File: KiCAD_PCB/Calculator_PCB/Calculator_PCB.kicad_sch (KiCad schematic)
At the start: 105 parts

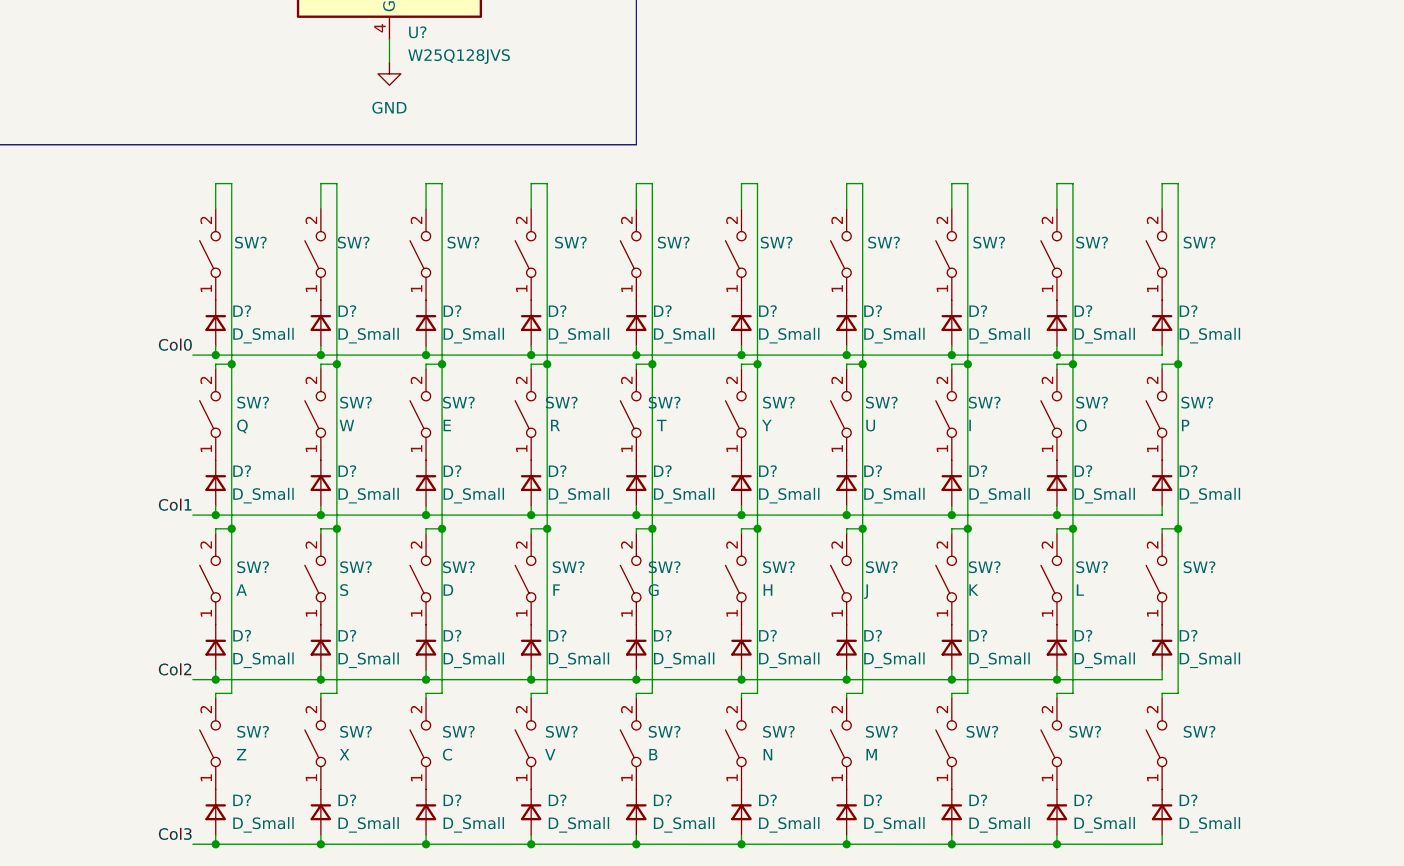
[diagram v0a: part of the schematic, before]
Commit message: PCB Updates
Defining Matrix
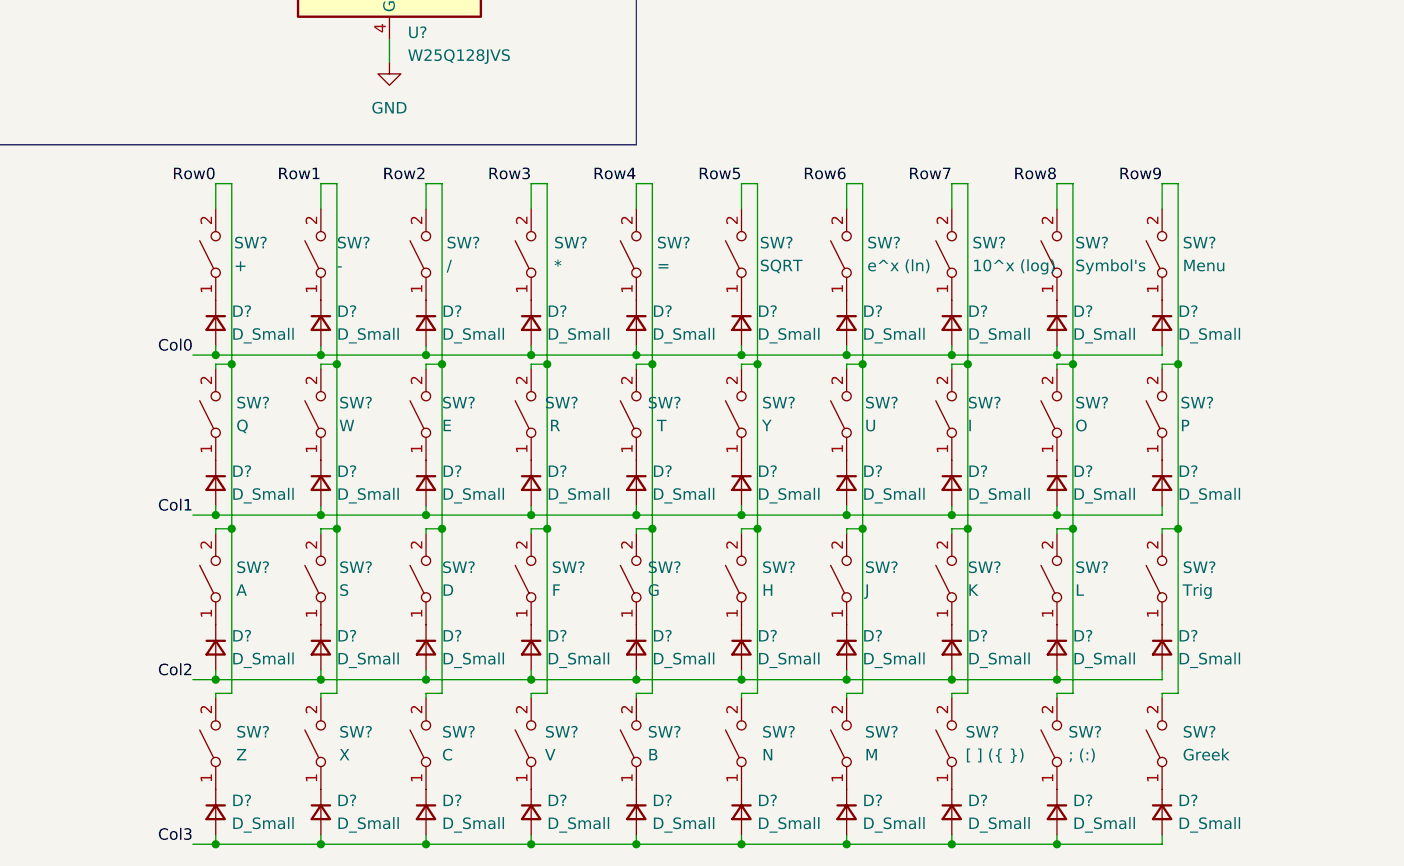
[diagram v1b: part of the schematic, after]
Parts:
- SW?: value (none) -> *
- SW?: value (none) -> ; (:)
- SW?: value (none) -> -
- SW?: value (none) -> Menu
- SW?: value (none) -> SQRT
- SW?: value (none) -> Trig
- SW?: value (none) -> Greek
- SW?: value (none) -> Symbol's
- SW?: value (none) -> e^x (ln)
- SW?: value (none) -> =
- SW?: value (none) -> /
- SW?: value (none) -> [ ] ({ })
- SW?: value (none) -> 10^x (log)
- SW?: value (none) -> +
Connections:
- net Row6: now reaches SW?.2 (B), SW?.2 (B), SW?.2 (B), SW?.2 (B)
- net Row0: now reaches SW?.2 (B), SW?.2 (B), SW?.2 (B), SW?.2 (B)
- net Row3: now reaches SW?.2 (B), SW?.2 (B), SW?.2 (B), SW?.2 (B)
- net Row8: now reaches SW?.2 (B), SW?.2 (B), SW?.2 (B), SW?.2 (B)
- net Row4: now reaches SW?.2 (B), SW?.2 (B), SW?.2 (B), SW?.2 (B)
- net Row1: now reaches SW?.2 (B), SW?.2 (B), SW?.2 (B), SW?.2 (B)
- net Row5: now reaches SW?.2 (B), SW?.2 (B), SW?.2 (B), SW?.2 (B)
- net Row9: now reaches SW?.2 (B), SW?.2 (B), SW?.2 (B), SW?.2 (B)
- net Row2: now reaches SW?.2 (B), SW?.2 (B), SW?.2 (B), SW?.2 (B)
- net Row7: now reaches SW?.2 (B), SW?.2 (B), SW?.2 (B), SW?.2 (B)
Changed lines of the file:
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@@
+    (effects (font (size 1.27 1.27)) (justify right bottom))
+  )
+  (label "Row6" (at 107.442 120.142 180)
+    (effects (font (size 1.27 1.27)) (justify right bottom))
+  )
+  (label "Row2" (at 60.706 120.142 180)
     (effects (font (size 1.27 1.27)) (justify right bottom))
   )
@@
     (effects (font (size 1.27 1.27)) (justify left bottom))
   )
+  (label "Row0" (at 37.338 120.142 180)
+    (effects (font (size 1.27 1.27)) (justify right bottom))
+  )
   (label "Col1" (at 34.798 156.972 180)
     (effects (font (size 1.27 1.27)) (justify right bottom))
@@
     (effects (font (size 1.27 1.27)) (justify left bottom))
   )
+  (label "Row5" (at 95.758 120.142 180)
+    (effects (font (size 1.27 1.27)) (justify right bottom))
+  )
   (label "XIN" (at 272.542 29.972 0)
     (effects (font (size 1.27 1.27)) (justify left bottom))
   )
+  (label "Row1" (at 49.022 120.142 180)
+    (effects (font (size 1.27 1.27)) (justify right bottom))
+  )
+  (label "Row8" (at 130.81 120.142 180)
+    (effects (font (size 1.27 1.27)) (justify right bottom))
+  )
   (label "QSPI_SCLK" (at 33.782 96.52 0)
     (effects (font (size 1.27 1.27)) (justify left bottom))
@@
     (effects (font (size 1.27 1.27)) (justify left bottom))
   )
+  (label "Row3" (at 72.39 120.142 180)
+    (effects (font (size 1.27 1.27)) (justify right bottom))
+  )
   (label "Col2" (at 34.798 175.26 180)
     (effects (font (size 1.27 1.27)) (justify right bottom))
   )
+  (label "Row9" (at 142.494 120.142 180)
+    (effects (font (size 1.27 1.27)) (justify right bottom))
+  )
+  (label "Row7" (at 119.126 120.142 180)
+    (effects (font (size 1.27 1.27)) (justify right bottom))
+  )
   (label "XOUT" (at 272.542 37.084 0)
     (effects (font (size 1.27 1.27)) (justify left bottom))
@@
   (label "USB_D-" (at 276.86 108.458 0)
     (effects (font (size 1.27 1.27)) (justify left bottom))
+  )
+  (label "Row4" (at 84.074 120.142 180)
+    (effects (font (size 1.27 1.27)) (justify right bottom))
   )
   (global_label "IOVDD_49" (shape input) (at 250.698 100.838 0) (fields_autoplaced)
@@
       (effects (font (size 1.27 1.27)) (justify right))
     )
-    (property "Value" "" (id 1) (at 74.93 129.286 90)
+    (property "Value" "*" (id 1) (at 74.93 129.286 90)
       (effects (font (size 1.27 1.27)) (justify right))
     )
@@
       (effects (font (size 1.27 1.27)) (justify right))
     )
-    (property "Value" "" (id 1) (at 132.08 183.6419 90)
+    (property "Value" "; (:)" (id 1) (at 132.08 183.6419 90)
       (effects (font (size 1.27 1.27)) (justify right))
     )
@@
       (effects (font (size 1.27 1.27)) (justify right))
     )
-    (property "Value" "" (id 1) (at 50.8 129.2859 90)
+    (property "Value" "-" (id 1) (at 50.8 129.2859 90)
       (effects (font (size 1.27 1.27)) (justify right))
     )
@@
       (effects (font (size 1.27 1.27)) (justify right))
     )
-    (property "Value" "" (id 1) (at 144.78 129.2859 90)
+    (property "Value" "Menu" (id 1) (at 144.78 129.2859 90)
       (effects (font (size 1.27 1.27)) (justify right))
     )
@@
       (effects (font (size 1.27 1.27)) (justify right))
     )
-    (property "Value" "" (id 1) (at 97.79 129.2859 90)
+    (property "Value" "SQRT" (id 1) (at 97.79 129.2859 90)
       (effects (font (size 1.27 1.27)) (justify right))
     )
@@
       (effects (font (size 1.27 1.27)) (justify right))
     )
-    (property "Value" "" (id 1) (at 144.78 165.3539 90)
+    (property "Value" "Trig" (id 1) (at 144.78 165.3539 90)
       (effects (font (size 1.27 1.27)) (justify right))
     )
@@
       (effects (font (size 1.27 1.27)) (justify right))
     )
-    (property "Value" "" (id 1) (at 144.78 183.6419 90)
+    (property "Value" "Greek" (id 1) (at 144.78 183.6419 90)
       (effects (font (size 1.27 1.27)) (justify right))
     )
@@
       (effects (font (size 1.27 1.27)) (justify right))
     )
-    (property "Value" "" (id 1) (at 132.842 129.286 90)
+    (property "Value" "Symbol's" (id 1) (at 132.842 129.286 90)
       (effects (font (size 1.27 1.27)) (justify right))
     )
@@
       (effects (font (size 1.27 1.27)) (justify right))
     )
-    (property "Value" "" (id 1) (at 109.728 129.286 90)
+    (property "Value" "e^x (ln)" (id 1) (at 109.728 129.286 90)
       (effects (font (size 1.27 1.27)) (justify right))
     )
@@
       (effects (font (size 1.27 1.27)) (justify right))
     )
-    (property "Value" "" (id 1) (at 86.36 129.2859 90)
+    (property "Value" "=" (id 1) (at 86.36 129.2859 90)
       (effects (font (size 1.27 1.27)) (justify right))
     )
@@
       (effects (font (size 1.27 1.27)) (justify right))
     )
-    (property "Value" "" (id 1) (at 62.992 129.286 90)
+    (property "Value" "/" (id 1) (at 62.992 129.286 90)
       (effects (font (size 1.27 1.27)) (justify right))
     )
@@
       (effects (font (size 1.27 1.27)) (justify right))
     )
-    (property "Value" "" (id 1) (at 120.65 183.6419 90)
+    (property "Value" "[ ] ({ })" (id 1) (at 120.65 183.6419 90)
       (effects (font (size 1.27 1.27)) (justify right))
     )
@@
       (effects (font (size 1.27 1.27)) (justify right))
     )
-    (property "Value" "" (id 1) (at 121.412 129.286 90)
+    (property "Value" "10^x (log)" (id 1) (at 121.412 129.286 90)
       (effects (font (size 1.27 1.27)) (justify right))
     )
@@
       (effects (font (size 1.27 1.27)) (justify right))
     )
-    (property "Value" "" (id 1) (at 39.37 129.2859 90)
-      (effects (font (size 1.27 1.27)) (justify right))
-    )
+    (property "Value" "+" (id 1) (at 39.37 129.2859 90)
+      (effects (font (size 1.27 1.27)) (justify right))
+    )

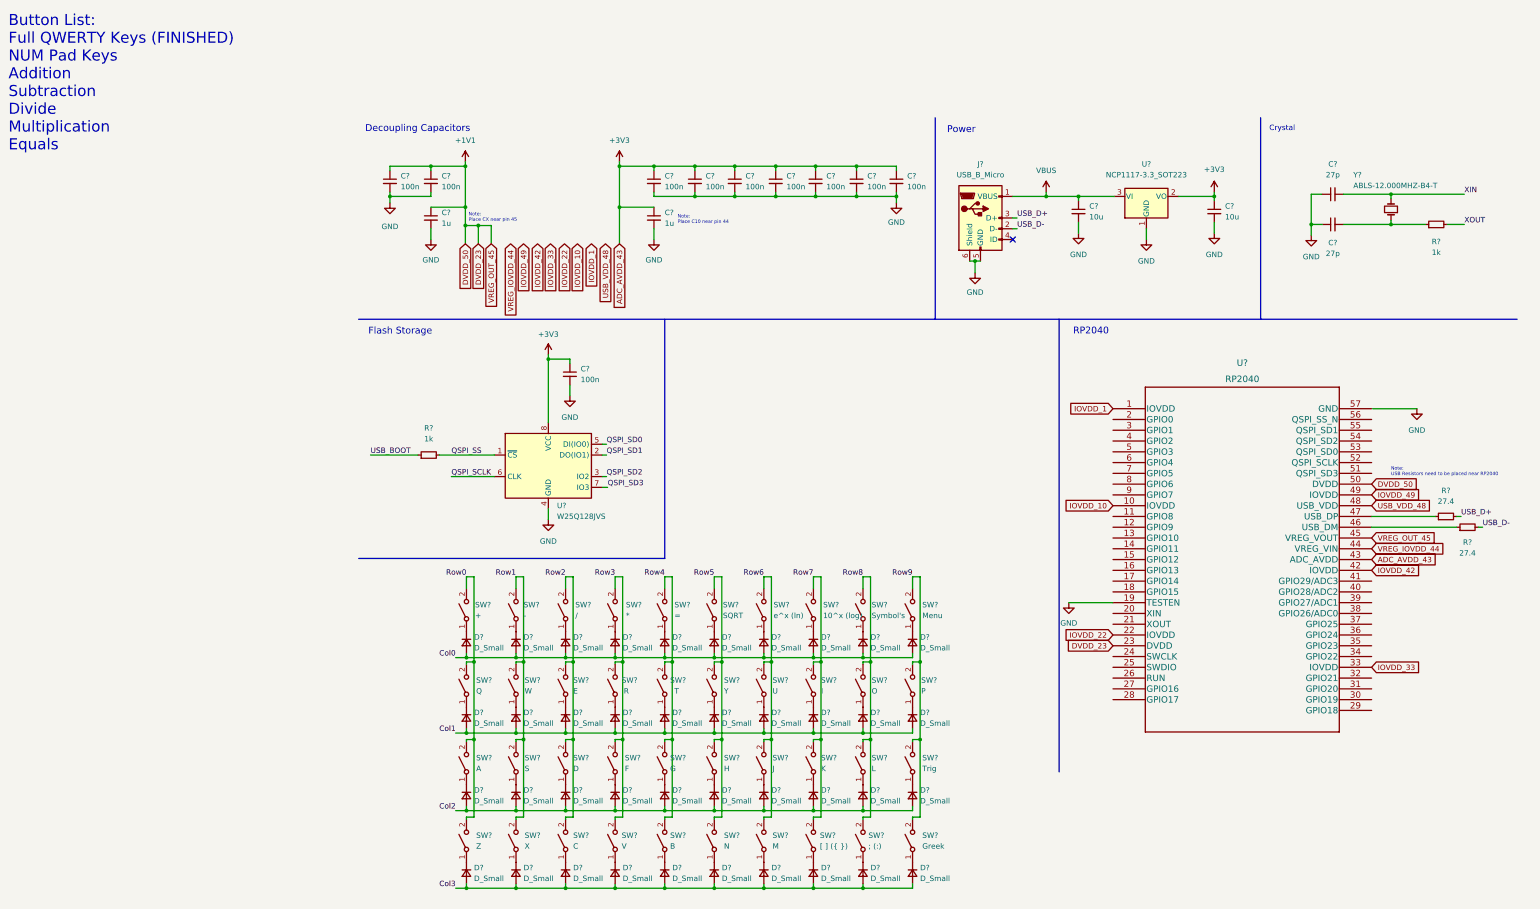
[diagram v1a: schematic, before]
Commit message: PCB Updates
Annotations added
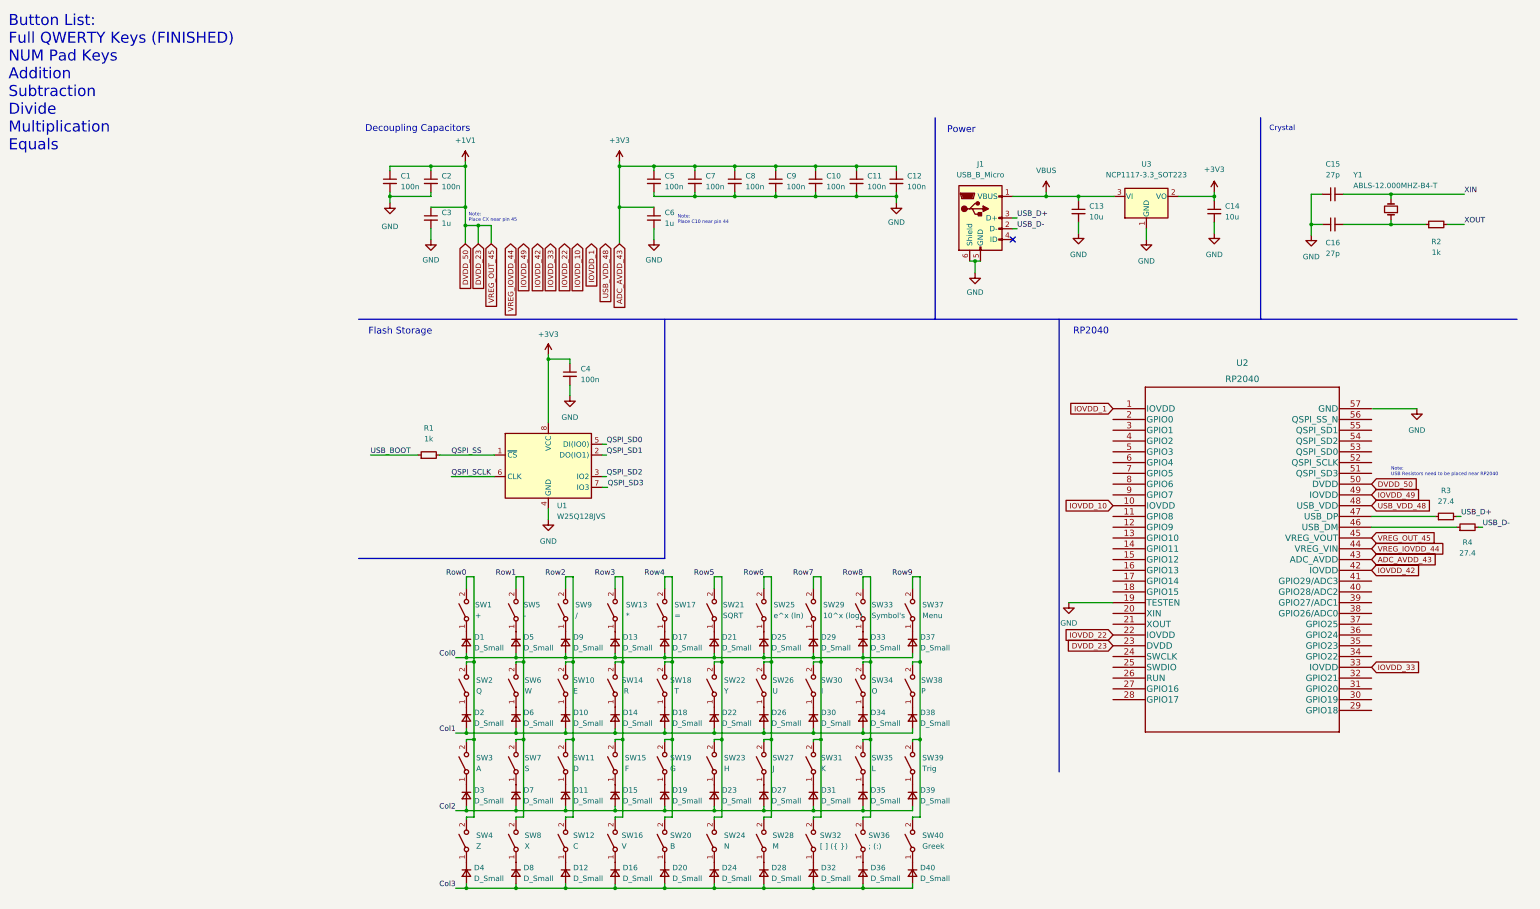
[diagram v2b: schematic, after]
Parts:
- gave numbers to parts that had none: 105

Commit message: PCB Updates
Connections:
- net IOVDD_1 is gone; now on net +3V3: U2.1 (IOVDD)
- net IOVDD_10 is gone; now on net +3V3: U2.10 (IOVDD)
- net IOVDD_22 is gone; now on net +3V3: U2.22 (IOVDD)
- net IOVDD_33 is gone; now on net +3V3: U2.33 (IOVDD)
- net IOVDD_42 is gone; now on net +3V3: U2.42 (IOVDD)
- net IOVDD_49 is gone; now on net +3V3: U2.49 (IOVDD)
- net USB_VDD_48 is gone; now on net +3V3: U2.48 (USB_VDD)
- net VREG_IOVDD_44 is gone; now on net +3V3: U2.44 (VREG_VIN)
- net GND: now also U2.57 (GND)

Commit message: PCB Updates
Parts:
- added R?: (no value), symbol Device:R_Small
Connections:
- net +3V3: now also R?.1
- net QSPI_SS: now also R?.2
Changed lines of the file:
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@@
   (junction (at 37.084 37.338) (diameter 0) (color 0 0 0 0)
   )
+  (junction (at 42.672 91.44) (diameter 0) (color 0 0 0 0)
+  )
   (junction (at 39.116 140.208) (diameter 0) (color 0 0 0 0)
   )
@@
   (junction (at 72.39 139.192) (diameter 0) (color 0 0 0 0)
   )
+  (junction (at 56.642 74.93) (diameter 0) (color 0 0 0 0)
+  )
   (junction (at 97.536 158.496) (diameter 0) (color 0 0 0 0)
   )
@@
     (stroke (width 0) (type default) (color 0 0 0 0))
   )
+  (wire (pts (xy 42.672 81.026) (xy 42.672 91.44))
+    (stroke (width 0) (type default) (color 0 0 0 0))
+  )
   (wire (pts (xy 179.324 126.238) (xy 189.738 126.238))
     (stroke (width 0) (type default) (color 0 0 0 0))
@@
     (stroke (width 0) (type default) (color 0 0 0 0))
   )
-  (wire (pts (xy 30.988 91.44) (xy 43.942 91.44))
+  (wire (pts (xy 30.988 91.44) (xy 42.672 91.44))
     (stroke (width 0) (type default) (color 0 0 0 0))
   )
@@
     (stroke (width 0) (type default) (color 0 0 0 0))
   )
+  (wire (pts (xy 56.642 74.93) (xy 56.642 83.82))
+    (stroke (width 0) (type default) (color 0 0 0 0))
+  )
   (wire (pts (xy 213.614 36.576) (xy 213.614 39.116))
     (stroke (width 0) (type default) (color 0 0 0 0))
@@
     (stroke (width 0) (type default) (color 0 0 0 0))
   )
-  (wire (pts (xy 56.642 68.834) (xy 56.642 83.82))
+  (wire (pts (xy 56.642 68.834) (xy 56.642 74.93))
     (stroke (width 0) (type default) (color 0 0 0 0))
   )
@@
     (stroke (width 0) (type default) (color 0 0 0 0))
   )
+  (wire (pts (xy 42.672 75.946) (xy 42.672 74.93))
+    (stroke (width 0) (type default) (color 0 0 0 0))
+  )
   (wire (pts (xy 60.706 174.244) (xy 60.706 175.26))
     (stroke (width 0) (type default) (color 0 0 0 0))
@@
     (stroke (width 0) (type default) (color 0 0 0 0))
   )
+  (wire (pts (xy 42.672 74.93) (xy 56.642 74.93))
+    (stroke (width 0) (type default) (color 0 0 0 0))
+  )
   (wire (pts (xy 60.706 139.192) (xy 72.39 139.192))
     (stroke (width 0) (type default) (color 0 0 0 0))
@@
     (stroke (width 0) (type default) (color 0 0 0 0))
   )
+  (wire (pts (xy 42.672 91.44) (xy 43.942 91.44))
+    (stroke (width 0) (type default) (color 0 0 0 0))
+  )
   (wire (pts (xy 60.452 37.338) (xy 57.15 37.338))
     (stroke (width 0) (type default) (color 0 0 0 0))
@@
     (pin "1")
   )
+  (symbol (lib_id "Device:R_Small") (at 42.672 78.486 0) (unit 1)
+    (in_bom yes) (on_board yes) (fields_autoplaced)
+    (property "Reference" "R?" (id 0) (at 44.45 77.2159 0)
+      (effects (font (size 1.27 1.27)) (justify left))
+    )
+    (property "Value" "" (id 1) (at 44.45 79.7559 0)
+      (effects (font (size 1.27 1.27)) (justify left))
+    )
+    (property "Footprint" "" (id 2) (at 42.672 78.486 0)
+      (effects (font (size 1.27 1.27)) hide)
+    )
+    (property "Datasheet" "~" (id 3) (at 42.672 78.486 0)
+      (effects (font (size 1.27 1.27)) hide)
+    )
+    (pin "1")
+    (pin "2")
+  )
   (symbol (lib_id "Switch:SW_SPST") (at 60.706 128.016 90) (unit 1)
     (in_bom yes) (on_board yes)
@@
       (reference "R4") (unit 1) (value "27.4") (footprint "")
     )
+    (path "/d5d4d22f-257e-4876-9315-653778a1c943"
+      (reference "R?") (unit 1) (value "10k") (footprint "")
+    )
     (path "/ea86cc11-be9d-452d-87f6-5ce1008e2886"
